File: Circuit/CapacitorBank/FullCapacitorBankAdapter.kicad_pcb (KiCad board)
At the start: 2 copper layers, 124.5 x 61 mm, 46 parts, among them J1 AC Power In, J2 Output+, J3 Output-, J4 To Control, T1 6:6:75+75, U1 L7812, U2 LM393, U3 LM393, U4 PC817

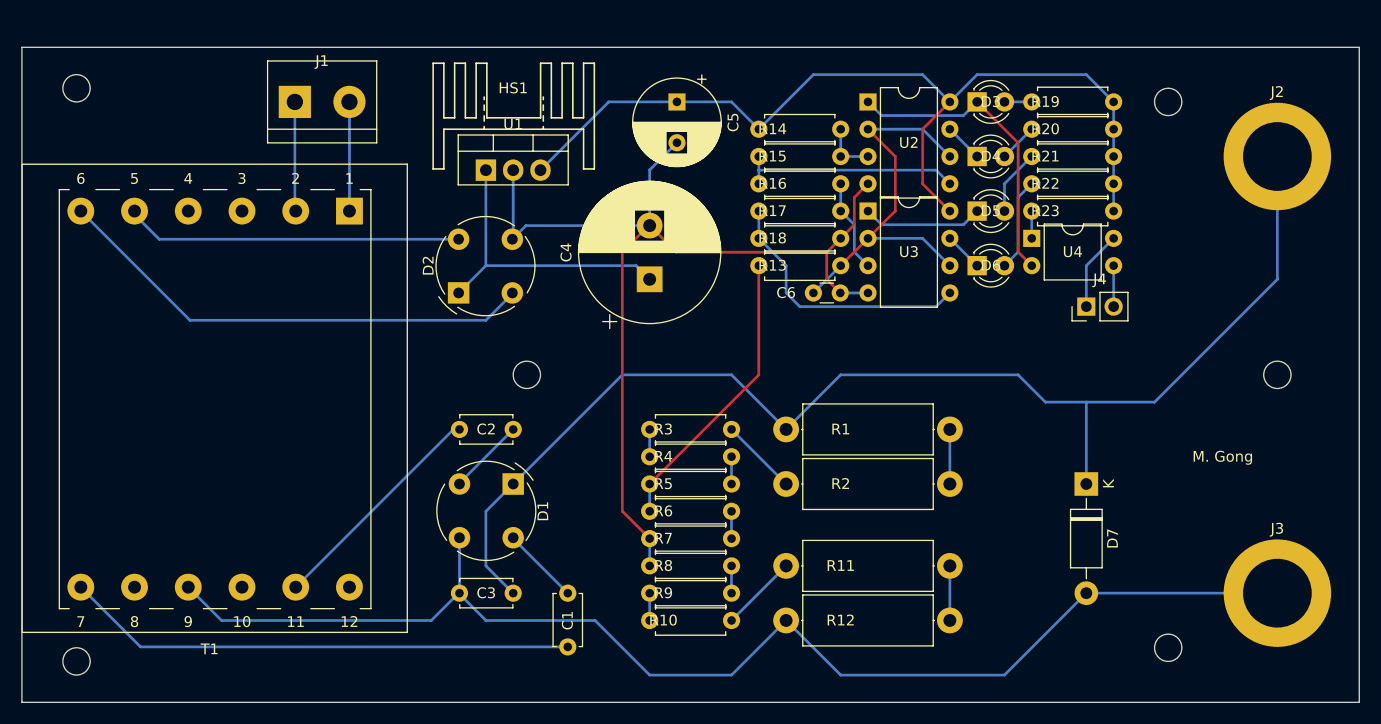
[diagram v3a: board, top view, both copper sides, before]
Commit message: [Circuit] Optimize the PCB layout of the capacitor bank adapter
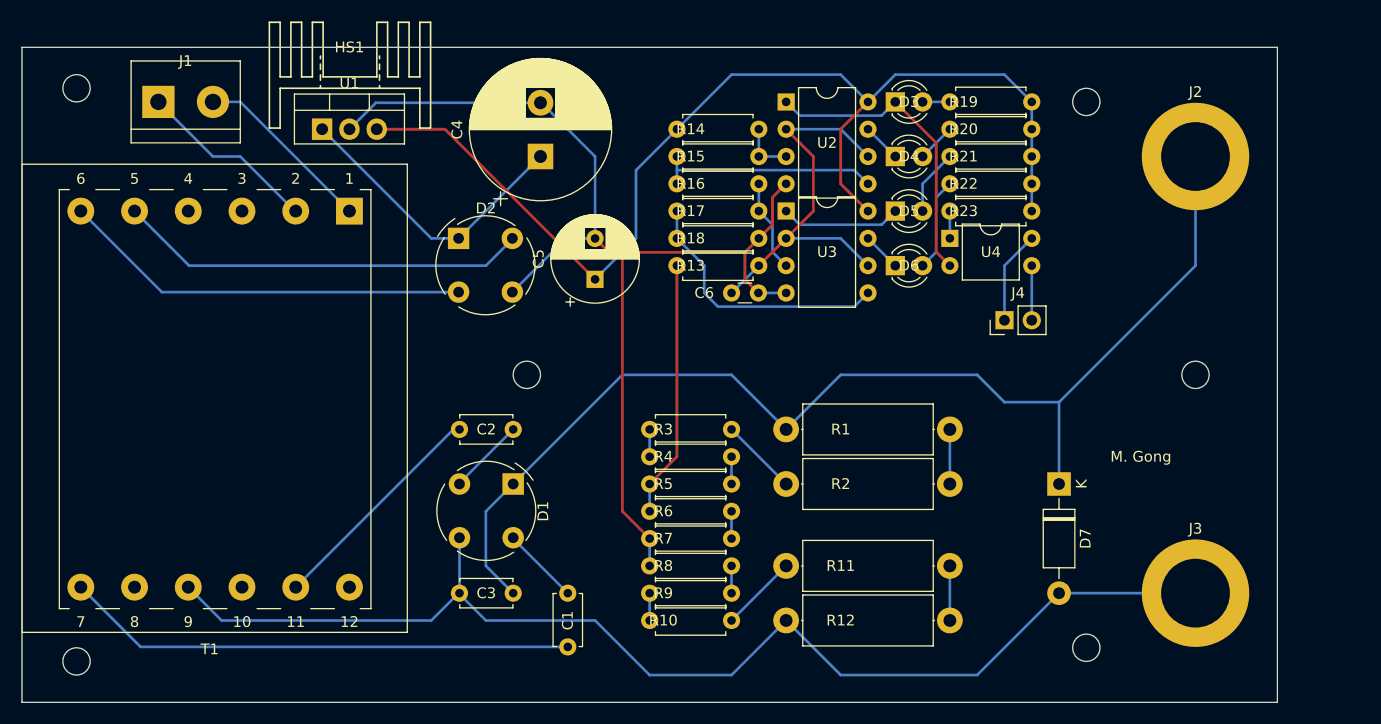
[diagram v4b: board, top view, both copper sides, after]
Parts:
- moved C5 18.2 mm to (101.6, 52.1), turned to 90 degrees
- moved HS1 15.7 mm to (78.7, 34.3)
- moved U1 15.7 mm to (76.2, 38.1)
- moved C4 15.3 mm to (96.5, 40.6)
- moved J1 12.7 mm to (61.0, 35.6)
- moved J4 7.73 mm to (139.7, 55.9)
- moved C6 7.62 mm to (114.3, 53.3)
- moved D3 7.62 mm to (129.5, 35.6)
- moved D4 7.62 mm to (129.5, 40.6)
- moved D5 7.62 mm to (129.5, 45.7)
- moved D6 7.62 mm to (129.5, 50.8)
- moved J2 7.62 mm to (157.5, 40.6)
- moved J3 7.62 mm to (157.5, 81.3)
- moved R15 7.62 mm to (109.2, 40.6)
- moved R17 7.62 mm to (109.2, 45.7)
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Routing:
- net +12V: track 84.7 -> 103.9 mm
- net /PowerOut+: track 116.6 -> 108.3 mm
- net GND: track 94.9 -> 103.0 mm
- net /PowerOut-: track 119.6 -> 112.0 mm
- net Net-(D2-Pad4): track 31.4 -> 39.0 mm
- net Net-(D2-Pad2): track 45.5 -> 38.3 mm
- net /ACPowerIn-: track 10.2 -> 17.0 mm
- net /ACPowerIn+: track 10.2 -> 16.9 mm
- net Net-(R13-Pad2): track 27.1 -> 23.9 mm
- net /ControlSignal: track 7.40 -> 8.67 mm
- net /ControlGND: track 3.81 -> 5.08 mm
- net Net-(C4-Pad1): track 28.2 -> 27.7 mm
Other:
- board size 124.5 x 61 mm -> 116.8 x 61 mm

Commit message: [Circuit] Add mini capacitor bank to the CapacitorBank schema
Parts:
- T1: value 6:6:75+75 -> 6:8:75+75
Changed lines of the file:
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@@
       (effects (font (size 1 1) (thickness 0.15)))
     )
-    (fp_text value 6:6:75+75 (at 13 -20) (layer F.Fab)
+    (fp_text value 6:8:75+75 (at 13 -20) (layer F.Fab)
       (effects (font (size 1 1) (thickness 0.15)))
     )

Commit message: [Circuit] Optimize the layout of PCBs
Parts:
- moved J4 10.2 mm to (129.5, 55.9)
- moved C5 3.81 mm to (101.6, 48.3), turned to 270 degrees
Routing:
- net /ControlSignal: track 8.67 -> 15.9 mm
- net /ControlGND: track 5.08 -> 12.3 mm
- net +12V: track 103.9 -> 98.5 mm
- net /PowerOut+: track 108.3 -> 110.4 mm
- net GND: track 103.0 -> 104.3 mm

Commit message: [Doc] Describe the updated design of control subsystem, and its interface
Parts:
- C1, C2, C3: value 1nF -> 1nF/1kV
- T1: value 6:8:75+75 -> 6:6:50+50
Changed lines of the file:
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@@
       (effects (font (size 1 1) (thickness 0.15)))
     )
-    (fp_text value 6:8:75+75 (at 13 -20) (layer F.Fab)
+    (fp_text value 6:6:50+50 (at 13 -20) (layer F.Fab)
       (effects (font (size 1 1) (thickness 0.15)))
     )
@@
       (effects (font (size 1 1) (thickness 0.15)))
     )
-    (fp_text value 1nF (at 2.5 -2.54 90) (layer F.Fab)
+    (fp_text value 1nF/1kV (at 2.5 -2.54 90) (layer F.Fab)
       (effects (font (size 1 1) (thickness 0.15)))
     )
@@
       (effects (font (size 1 1) (thickness 0.15)))
     )
-    (fp_text value 1nF (at 2.54 -2.54) (layer F.Fab)
+    (fp_text value 1nF/1kV (at 2.54 -2.54) (layer F.Fab)
       (effects (font (size 1 1) (thickness 0.15)))
     )
@@
       (effects (font (size 1 1) (thickness 0.15)))
     )
-    (fp_text value 1nF (at 2.5 2.5) (layer F.Fab)
-      (effects (font (size 1 1) (thickness 0.15)))
-    )
+    (fp_text value 1nF/1kV (at 2.5 2.5) (layer F.Fab)
+      (effects (font (size 1 1) (thickness 0.15)))
+    )
